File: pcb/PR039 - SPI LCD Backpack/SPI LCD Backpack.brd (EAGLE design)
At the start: 48.3 x 24.1 mm, 15 parts, among them IC1 74HC595D, T1 BC847, T2 BC847, T3 BC847, X1 22-23-2081

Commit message: 
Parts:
- moved C1 2.54 mm to (31.8, 12.7)
- moved C2 2.54 mm to (34.3, 12.7)
- moved IC1 2.54 mm to (25.4, 12.7)
- turned R2 to 180 degrees
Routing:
- net +5V: track 99.6 -> 89.8 mm
- net LED_1: track 8.47 -> 0.00 mm
- net N$5: track 11.4 -> 6.35 mm
- net CLOCK: track 8.25 -> 5.34 mm
- net RS: track 76.4 -> 78.5 mm
- net DB7: track 12.4 -> 14.3 mm
- net DB6: track 10.0 -> 12.0 mm
- net DB5: track 7.66 -> 9.57 mm
- net DB4: track 7.13 -> 9.04 mm
- net DATA: track 6.61 -> 4.81 mm
- net E: track 25.1 -> 26.7 mm
- net LATCH: track 5.86 -> 4.81 mm

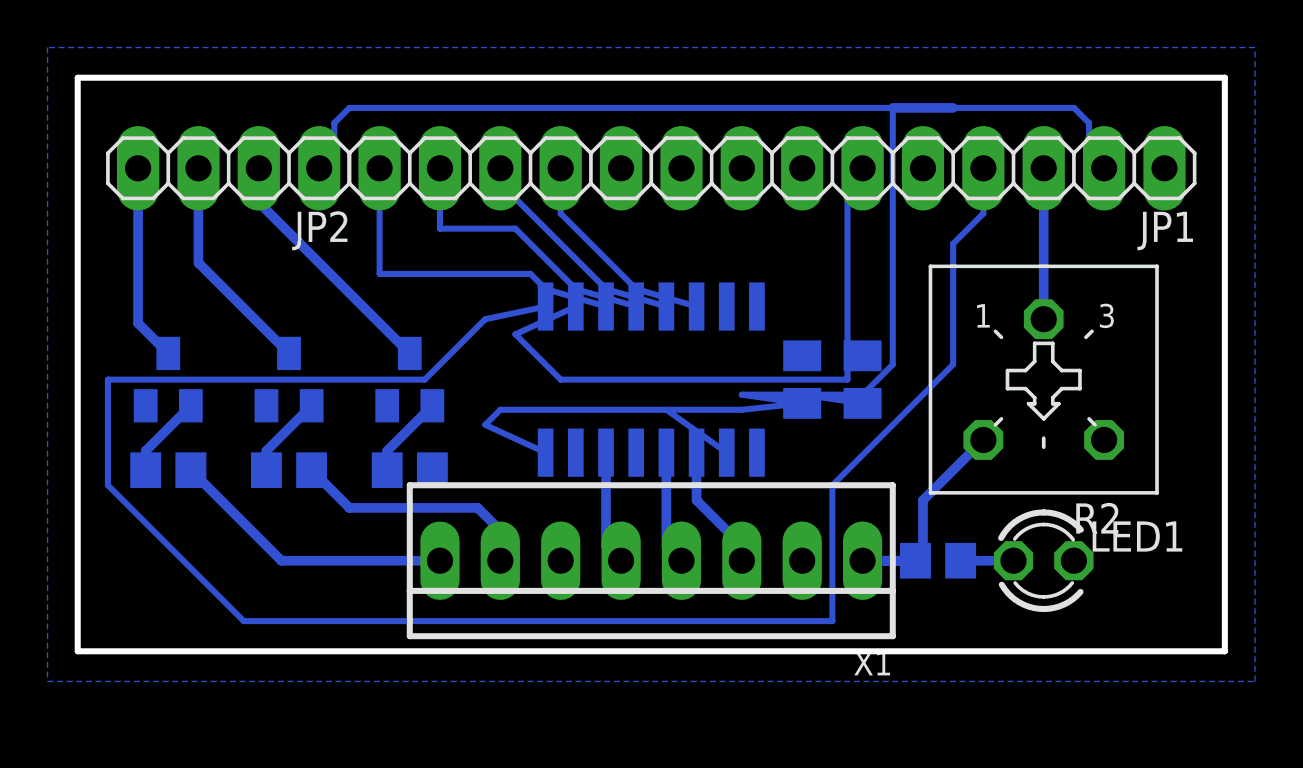
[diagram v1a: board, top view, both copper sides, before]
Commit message: 
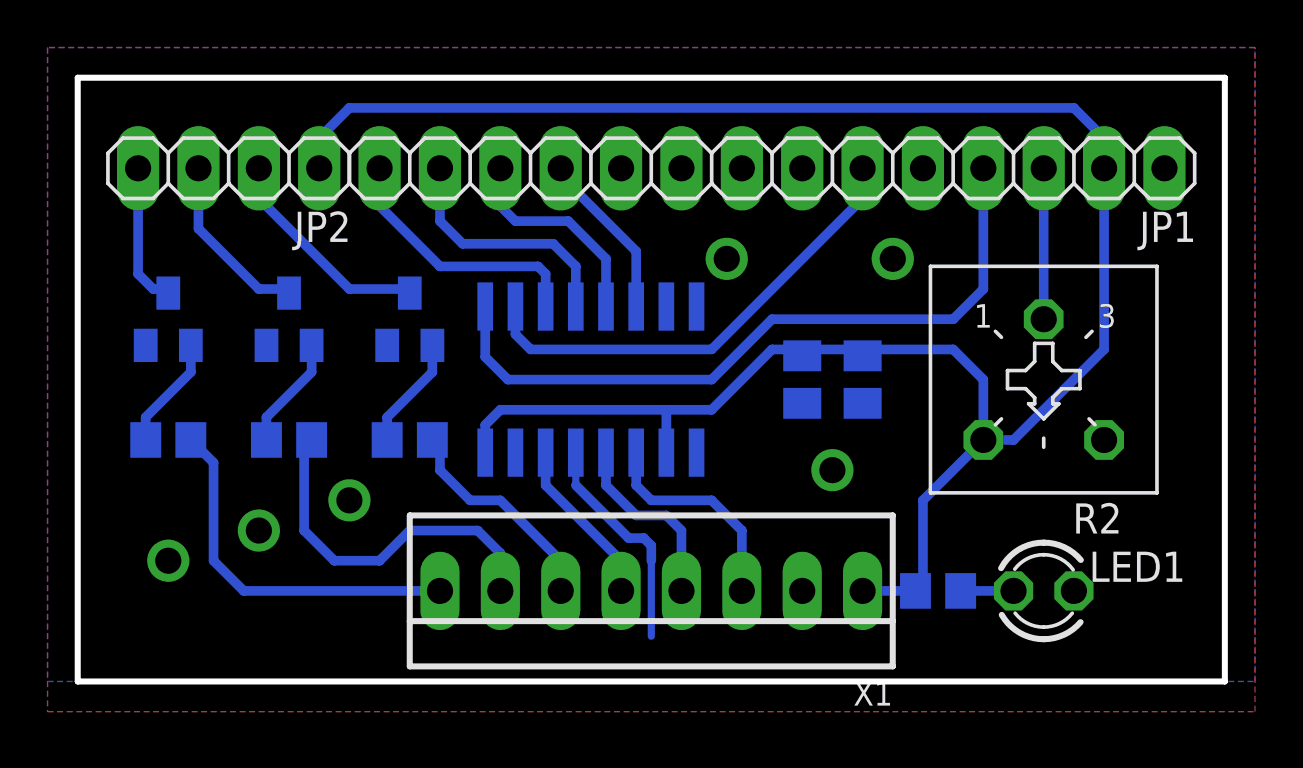
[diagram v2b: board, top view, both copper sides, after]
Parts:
- moved T1 2.54 mm to (15.2, 15.2)
- moved T2 2.54 mm to (10.2, 15.2)
- moved T3 2.54 mm to (5.08, 15.2)
- moved IC1 2.54 mm to (22.9, 12.7)
- moved LED1 1.27 mm to (41.9, 3.81)
- moved R1 1.27 mm to (37.5, 3.81)
- moved X1 1.27 mm to (25.4, 3.81)
- moved R3 1.27 mm to (15.2, 10.2)
- moved R4 1.27 mm to (10.2, 10.2)
- moved R5 1.27 mm to (5.08, 10.2)
- turned C1 to 270 degrees
- turned C2 to 270 degrees
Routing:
- net RS: track 78.5 -> 30.1 mm
- net GND: track 0.00 -> 9.41 mm, vias 0 -> 6
- net LED_1: track 0.00 -> 9.33 mm
- net E: track 26.7 -> 19.9 mm
- net LED_2: track 10.3 -> 15.2 mm
- net CLOCK: track 5.34 -> 9.15 mm
- net LED_3: track 12.1 -> 15.5 mm
- net DB7: track 14.3 -> 11.1 mm
- net LATCH: track 4.81 -> 7.88 mm
- net DATA: track 4.81 -> 7.13 mm
- net N$8: track 8.32 -> 6.05 mm
- net DB4: track 9.04 -> 7.13 mm
- net N$7: track 9.37 -> 7.47 mm
- net N$2: track 3.50 -> 5.23 mm
- net N$1: track 3.50 -> 5.23 mm
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- added copper zone on layer 1, net GND
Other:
- board size 48.3 x 24.1 mm -> 48.3 x 25.4 mm

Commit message: 
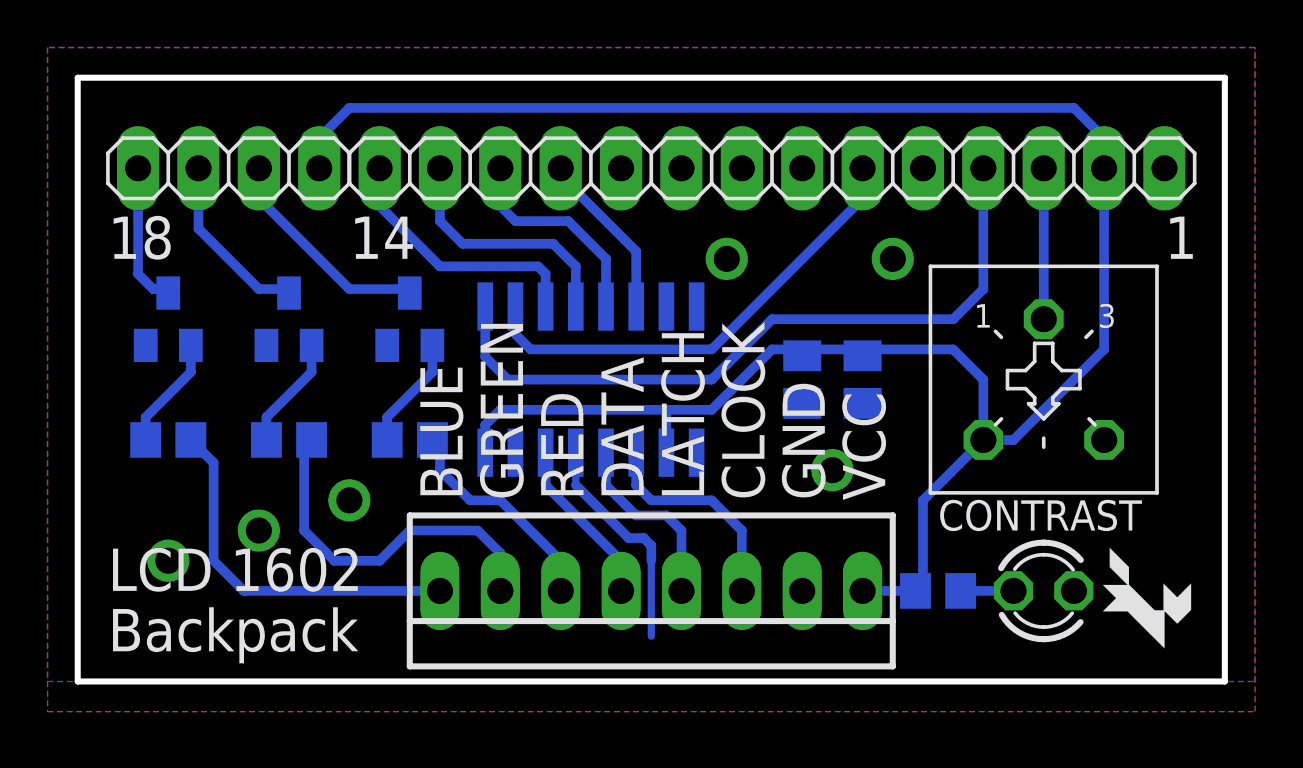
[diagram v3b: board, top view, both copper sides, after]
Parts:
- added U$1: (no value), SPI LCD Backpack:FOX-1
- X1: value 22-23-2081 -> (none)
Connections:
- net LED_1 renamed RED
- net LED_2 renamed GREEN
- net LED_3 renamed BLUE
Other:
- board text added: "BLUE"
- board text added: "Backpack"
- board text added: "CLOCK"
- board text added: "CONTRAST"
- board text added: "DATA"
- board text added: "GND"
- board text added: "GREEN"
- board text added: "LATCH"
- board text added: "LCD 1602"
- board text added: "RED"
- board text added: "VCC"
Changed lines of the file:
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@@
 <?xml version="1.0" encoding="utf-8"?>
 <!DOCTYPE eagle SYSTEM "eagle.dtd">
-<eagle version="6.6.0">
+<eagle version="6.5.0">
 <drawing>
 <settings>
@@
 <board>
 <plain>
-<wire x1="25.4" y1="25.4" x2="25.4" y2="0" width="0.4064" layer="49"/>
-<text x="46.99" y="24.13" size="1.778" layer="49">1</text>
-<text x="12.7" y="24.13" size="1.778" layer="49">14</text>
-<text x="2.54" y="24.13" size="1.778" layer="49">18</text>
+<text x="46.99" y="17.78" size="1.778" layer="25" font="vector" ratio="12">1</text>
+<text x="12.7" y="17.78" size="1.778" layer="25" font="vector" ratio="12">14</text>
+<text x="2.54" y="17.78" size="1.778" layer="25" font="vector" ratio="12">18</text>
 <wire x1="1.27" y1="0" x2="1.27" y2="25.4" width="0.254" layer="20"/>
 <wire x1="1.27" y1="25.4" x2="49.53" y2="25.4" width="0.254" layer="20"/>
 <wire x1="49.53" y1="25.4" x2="49.53" y2="0" width="0.254" layer="20"/>
 <wire x1="49.53" y1="0" x2="1.27" y2="0" width="0.254" layer="20"/>
-<dimension x1="1.27" y1="25.4" x2="49.53" y2="25.4" x3="25.4" y3="27.94" textsize="1.778" layer="49"/>
-<dimension x1="1.27" y1="0" x2="1.27" y2="25.4" x3="-1.27" y3="12.7" textsize="1.778" layer="49"/>
+<dimension x1="1.27" y1="25.4" x2="49.53" y2="25.4" x3="25.4" y3="27.94" textsize="1.778" textratio="12" layer="49"/>
+<dimension x1="1.27" y1="0" x2="1.27" y2="25.4" x3="-1.27" y3="12.7" textsize="1.778" textratio="12" layer="49"/>
+<text x="2.54" y="3.81" size="1.778" layer="21" font="vector" ratio="12">LCD 1602</text>
+<text x="2.54" y="1.27" size="1.778" layer="21" font="vector" ratio="12">Backpack</text>
+<text x="17.4625" y="7.62" size="1.778" layer="21" font="vector" ratio="12" rot="R90">BLUE</text>
+<text x="20.0025" y="7.62" size="1.778" layer="21" font="vector" ratio="12" rot="R90">GREEN</text>
+<text x="22.5425" y="7.62" size="1.778" layer="21" font="vector" ratio="12" rot="R90">RED</text>
+<text x="25.0825" y="7.62" size="1.778" layer="21" font="vector" ratio="12" rot="R90">DATA</text>
+<text x="30.1625" y="7.62" size="1.778" layer="21" font="vector" ratio="12" rot="R90">CLOCK</text>
+<text x="27.6225" y="7.62" size="1.778" layer="21" font="vector" ratio="12" rot="R90">LATCH</text>
+<text x="35.2425" y="7.62" size="1.778" layer="21" font="vector" ratio="12" rot="R90">VCC</text>
+<text x="32.7025" y="7.62" size="1.778" layer="21" font="vector" ratio="12" rot="R90">GND</text>
+<text x="37.465" y="6.35" size="1.27" layer="21" font="vector" ratio="12">CONTRAST</text>
 </plain>
 <attributes>
@@
 </autorouter>
 <elements>
-<element name="C1" library="SPI LCD Backpack" package="C0805K" value="" x="31.75" y="12.7" rot="MR270"/>
-<element name="R1" library="SPI LCD Backpack" package="R0805" value="" x="37.465" y="3.81" rot="MR0"/>
-<element name="IC1" library="SPI LCD Backpack" package="SO16" value="74HC595D" x="22.86" y="12.7" rot="MR180"/>
-<element name="JP1" library="SPI LCD Backpack" package="1X14" value="" x="30.48" y="21.59" rot="R180"/>
-<element name="LED1" library="SPI LCD Backpack" package="LED3MM" value="" x="41.91" y="3.81"/>
-<element name="C2" library="SPI LCD Backpack" package="C0805K" value="" x="34.29" y="12.7" rot="MR270"/>
-<element name="R2" library="SPI LCD Backpack" package="3386F" value="" x="41.91" y="12.7" rot="R180"/>
-<element name="R3" library="SPI LCD Backpack" package="R0805" value="" x="15.24" y="10.16" rot="MR0"/>
-<element name="T1" library="SPI LCD Backpack" package="SOT23" value="BC847" x="15.24" y="15.24" rot="MR0"/>
-<element name="R4" library="SPI LCD Backpack" package="R0805" value="" x="10.16" y="10.16" rot="MR0"/>
-<element name="T2" library="SPI LCD Backpack" package="SOT23" value="BC847" x="10.16" y="15.24" rot="MR0"/>
-<element name="R5" library="SPI LCD Backpack" package="R0805" value="" x="5.08" y="10.16" rot="MR0"/>
-<element name="T3" library="SPI LCD Backpack" package="SOT23" value="BC847" x="5.08" y="15.24" rot="MR0"/>
-<element name="JP2" library="SPI LCD Backpack" package="1X04" value="" x="7.62" y="21.59" rot="R180"/>
-<element name="X1" library="SPI LCD Backpack" package="22-23-2081" value="22-23-2081" x="25.4" y="3.81" rot="R180">
+<element name="C1" library="SPI LCD Backpack" package="C0805K" value="" x="31.75" y="12.7" smashed="yes" rot="MR270">
+<attribute name="VALUE" x="33.65" y="13.7" size="1.016" layer="28" rot="MR270"/>
+</element>
+<element name="R1" library="SPI LCD Backpack" package="R0805" value="" x="37.465" y="3.81" smashed="yes" rot="MR0">
+<attribute name="VALUE" x="38.1" y="1.27" size="1.27" layer="28" rot="MR0"/>
+</element>
+<element name="IC1" library="SPI LCD Backpack" package="SO16" value="74HC595D" x="22.86" y="12.7" smashed="yes" rot="MR180"/>
+<element name="JP1" library="SPI LCD Backpack" package="1X14" value="" x="30.48" y="21.59" smashed="yes" rot="R180">
+<attribute name="VALUE" x="48.26" y="24.765" size="1.27" layer="27" rot="R180"/>
+</element>
+<element name="LED1" library="SPI LCD Backpack" package="LED3MM" value="" x="41.91" y="3.81" smashed="yes">
+<attribute name="VALUE" x="43.815" y="2.159" size="1.27" layer="27" ratio="10"/>
+</element>
+<element name="C2" library="SPI LCD Backpack" package="C0805K" value="" x="34.29" y="12.7" smashed="yes" rot="MR270">
+<attribute name="VALUE" x="36.19" y="13.7" size="1.016" layer="28" rot="MR270"/>
+</element>
+<element name="R2" library="SPI LCD Backpack" package="3386F" value="" x="41.91" y="12.7" smashed="yes" rot="R180">
+<attribute name="VALUE" x="45.1866" y="19.177" size="1.27" layer="27" ratio="10" rot="R180"/>
+</element>
+<element name="R3" library="SPI LCD Backpack" package="R0805" value="" x="15.24" y="10.16" smashed="yes" rot="MR0">
+<attribute name="VALUE" x="15.875" y="7.62" size="1.27" layer="28" rot="MR0"/>
+</element>
+<element name="T1" library="SPI LCD Backpack" package="SOT23" value="BC847" x="15.24" y="15.24" smashed="yes" rot="MR0"/>
+<element name="R4" library="SPI LCD Backpack" package="R0805" value="" x="10.16" y="10.16" smashed="yes" rot="MR0">
+<attribute name="VALUE" x="10.795" y="7.62" size="1.27" layer="28" rot="MR0"/>
+</element>
+<element name="T2" library="SPI LCD Backpack" package="SOT23" value="BC847" x="10.16" y="15.24" smashed="yes" rot="MR0"/>
+<element name="R5" library="SPI LCD Backpack" package="R0805" value="" x="5.08" y="10.16" smashed="yes" rot="MR0">
+<attribute name="VALUE" x="5.715" y="7.62" size="1.27" layer="28" rot="MR0"/>
+</element>
+<element name="T3" library="SPI LCD Backpack" package="SOT23" value="BC847" x="5.08" y="15.24" smashed="yes" rot="MR0"/>
+<element name="JP2" library="SPI LCD Backpack" package="1X04" value="" x="7.62" y="21.59" smashed="yes" rot="R180">
+<attribute name="VALUE" x="12.7" y="24.765" size="1.27" layer="27" rot="R180"/>
+</element>
+<element name="X1" library="SPI LCD Backpack" package="22-23-2081" value="" x="25.4" y="3.81" smashed="yes" rot="R180">
 <attribute name="OC_NEWARK" value="01C7592" x="25.4" y="3.81" size="1.778" layer="27" rot="R180" display="off"/>
 <attribute name="MPN" value="22-23-2081" x="25.4" y="3.81" size="1.778" layer="27" rot="R180" display="off"/>
@@
 <attribute name="OC_FARNELL" value="1756826" x="25.4" y="3.81" size="1.778" layer="27" rot="R180" display="off"/>
 </element>
+<element name="U$1" library="SPI LCD Backpack" package="FOX-1" value="" x="46.355" y="3.4925"/>
 </elements>
 <signals>
@@
 <wire x1="4.91" y1="16.51" x2="5.08" y2="16.34" width="0.4064" layer="16"/>
 </signal>
-<signal name="LED_1">
+<signal name="RED">
 <contactref element="R3" pad="1"/>
 <contactref element="X1" pad="6"/>
@@
 <wire x1="16.51" y1="9.84" x2="16.19" y2="10.16" width="0.4064" layer="16"/>
 </signal>
-<signal name="LED_2">
+<signal name="GREEN">
 <contactref element="R4" pad="1"/>
 <contactref element="X1" pad="7"/>
@@
 <wire x1="10.795" y1="9.845" x2="11.11" y2="10.16" width="0.4064" layer="16"/>
 </signal>
-<signal name="LED_3">
+<signal name="BLUE">
 <contactref element="R5" pad="1"/>
 <contactref element="X1" pad="8"/>

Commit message: 
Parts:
- C1: value (none) -> 1uF
- C2: value (none) -> 100nF
- R1: value (none) -> 1k
- R3, R4, R5: value (none) -> 10k
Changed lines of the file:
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@@
 <?xml version="1.0" encoding="utf-8"?>
 <!DOCTYPE eagle SYSTEM "eagle.dtd">
-<eagle version="6.5.0">
+<eagle version="7.1.0">
 <drawing>
 <settings>
@@
 <pass name="Default">
 <param name="RoutingGrid" value="25mil"/>
+<param name="AutoGrid" value="1"/>
+<param name="Efforts" value="0"/>
+<param name="TopRouterVariant" value="1"/>
 <param name="tpViaShape" value="round"/>
 <param name="PrefDir.1" value="0"/>
@@
 </autorouter>
 <elements>
-<element name="C1" library="SPI LCD Backpack" package="C0805K" value="" x="31.75" y="12.7" smashed="yes" rot="MR270">
-<attribute name="VALUE" x="33.65" y="13.7" size="1.016" layer="28" rot="MR270"/>
-</element>
-<element name="R1" library="SPI LCD Backpack" package="R0805" value="" x="37.465" y="3.81" smashed="yes" rot="MR0">
-<attribute name="VALUE" x="38.1" y="1.27" size="1.27" layer="28" rot="MR0"/>
-</element>
+<element name="C1" library="SPI LCD Backpack" package="C0805K" value="1uF" x="31.75" y="12.7" smashed="yes" rot="MR270"/>
+<element name="R1" library="SPI LCD Backpack" package="R0805" value="1k" x="37.465" y="3.81" smashed="yes" rot="MR0"/>
 <element name="IC1" library="SPI LCD Backpack" package="SO16" value="74HC595D" x="22.86" y="12.7" smashed="yes" rot="MR180"/>
 <element name="JP1" library="SPI LCD Backpack" package="1X14" value="" x="30.48" y="21.59" smashed="yes" rot="R180">
@@
 <attribute name="VALUE" x="43.815" y="2.159" size="1.27" layer="27" ratio="10"/>
 </element>
-<element name="C2" library="SPI LCD Backpack" package="C0805K" value="" x="34.29" y="12.7" smashed="yes" rot="MR270">
-<attribute name="VALUE" x="36.19" y="13.7" size="1.016" layer="28" rot="MR270"/>
-</element>
+<element name="C2" library="SPI LCD Backpack" package="C0805K" value="100nF" x="34.29" y="12.7" smashed="yes" rot="MR270"/>
 <element name="R2" library="SPI LCD Backpack" package="3386F" value="" x="41.91" y="12.7" smashed="yes" rot="R180">
 <attribute name="VALUE" x="45.1866" y="19.177" size="1.27" layer="27" ratio="10" rot="R180"/>
 </element>
-<element name="R3" library="SPI LCD Backpack" package="R0805" value="" x="15.24" y="10.16" smashed="yes" rot="MR0">
-<attribute name="VALUE" x="15.875" y="7.62" size="1.27" layer="28" rot="MR0"/>
-</element>
+<element name="R3" library="SPI LCD Backpack" package="R0805" value="10k" x="15.24" y="10.16" smashed="yes" rot="MR0"/>
 <element name="T1" library="SPI LCD Backpack" package="SOT23" value="BC847" x="15.24" y="15.24" smashed="yes" rot="MR0"/>
-<element name="R4" library="SPI LCD Backpack" package="R0805" value="" x="10.16" y="10.16" smashed="yes" rot="MR0">
-<attribute name="VALUE" x="10.795" y="7.62" size="1.27" layer="28" rot="MR0"/>
-</element>
+<element name="R4" library="SPI LCD Backpack" package="R0805" value="10k" x="10.16" y="10.16" smashed="yes" rot="MR0"/>
 <element name="T2" library="SPI LCD Backpack" package="SOT23" value="BC847" x="10.16" y="15.24" smashed="yes" rot="MR0"/>
-<element name="R5" library="SPI LCD Backpack" package="R0805" value="" x="5.08" y="10.16" smashed="yes" rot="MR0">
-<attribute name="VALUE" x="5.715" y="7.62" size="1.27" layer="28" rot="MR0"/>
-</element>
+<element name="R5" library="SPI LCD Backpack" package="R0805" value="10k" x="5.08" y="10.16" smashed="yes" rot="MR0"/>
 <element name="T3" library="SPI LCD Backpack" package="SOT23" value="BC847" x="5.08" y="15.24" smashed="yes" rot="MR0"/>
 <element name="JP2" library="SPI LCD Backpack" package="1X04" value="" x="7.62" y="21.59" smashed="yes" rot="R180">
